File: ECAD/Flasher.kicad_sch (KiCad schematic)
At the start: 7 parts, among them Q1 BC817, Q2 BC817, U3 CH340C

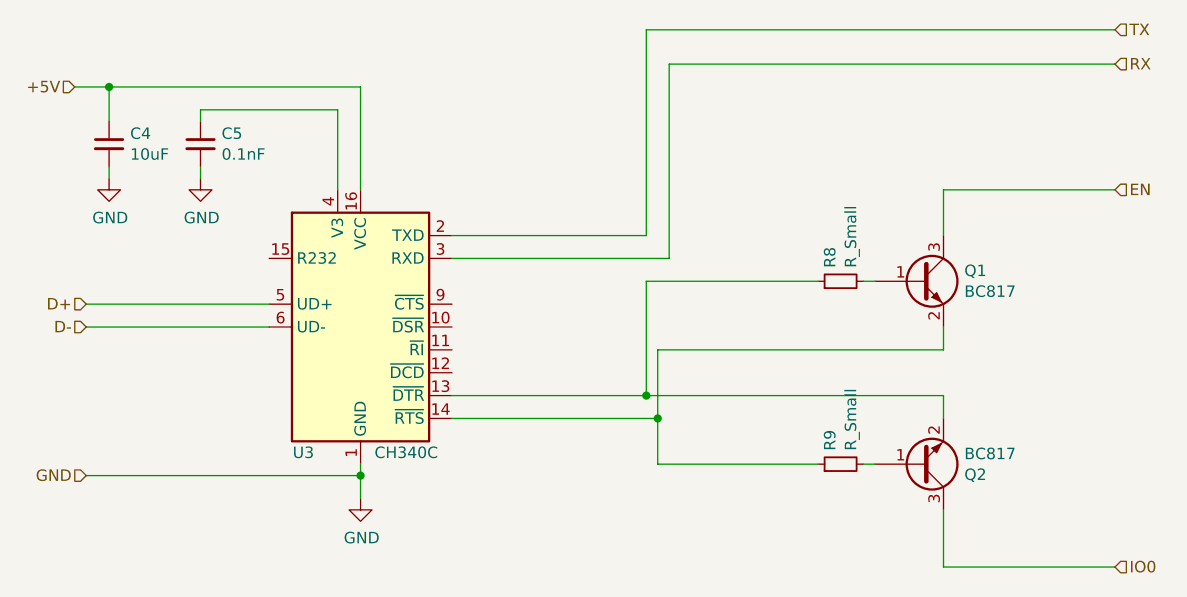
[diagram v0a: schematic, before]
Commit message: finishing up pcb, only billonly bill of materials need to be done to be compatible with lc from jlcpcb
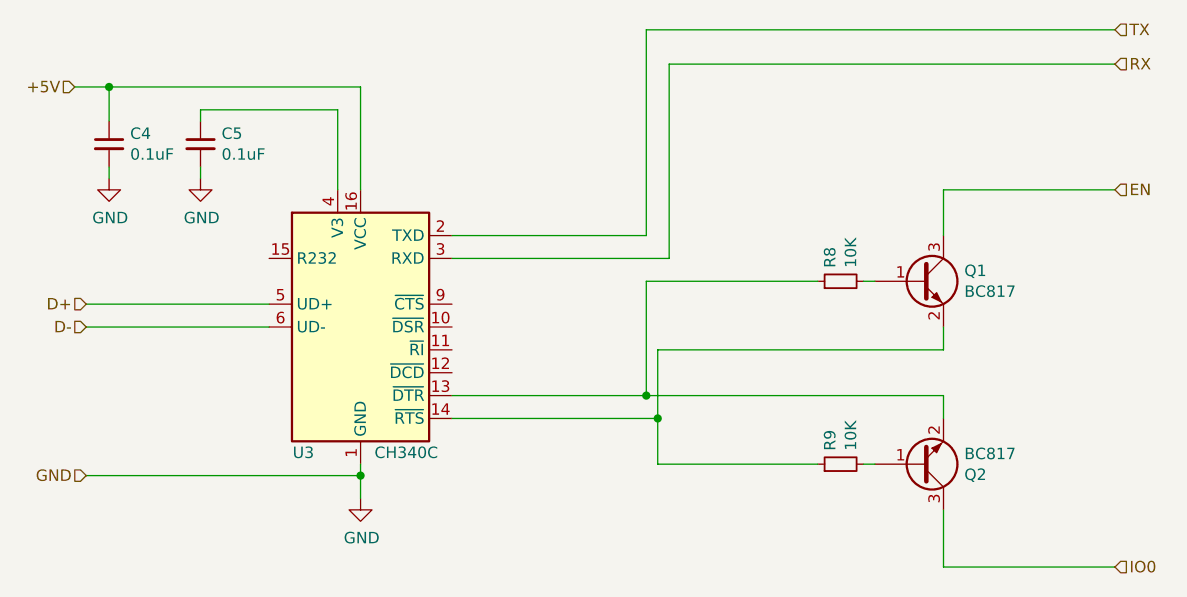
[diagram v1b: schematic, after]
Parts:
- C4: value 10uF -> 0.1uF
- C5: value 0.1nF -> 0.1uF
- R8, R9: value R_Small -> 10K
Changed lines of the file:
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@@
       (effects (font (size 1.27 1.27)) (justify left))
     )
-    (property "Value" "R_Small" (id 1) (at 129.413 79.7814 0)
+    (property "Value" "10K" (id 1) (at 129.413 79.781 0)
       (effects (font (size 1.27 1.27)) (justify left))
     )
@@
       (effects (font (size 1.27 1.27)) (justify left))
     )
-    (property "Value" "R_Small" (id 1) (at 129.413 100.1014 0)
+    (property "Value" "10K" (id 1) (at 129.413 100.1014 0)
       (effects (font (size 1.27 1.27)) (justify left))
     )
@@
       (effects (font (size 1.27 1.27)) (justify left))
     )
-    (property "Value" "10uF" (id 1) (at 49.3268 67.183 0)
+    (property "Value" "0.1uF" (id 1) (at 49.327 67.183 0)
       (effects (font (size 1.27 1.27)) (justify left))
     )
@@
       (effects (font (size 1.27 1.27)) (justify left))
     )
-    (property "Value" "0.1nF" (id 1) (at 59.4868 67.183 0)
+    (property "Value" "0.1uF" (id 1) (at 59.4868 67.183 0)
       (effects (font (size 1.27 1.27)) (justify left))
     )

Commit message: BOM fixed, ready to order
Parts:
- C4, C5: Manufacturer (none) -> CCTC; Manufacturer Number (none) -> TCC0603X7R104K500CT
- Q1, Q2: Manufacturer (none) -> ON Semiconductor; Manufacturer Number (none) -> BC818-40LT1G
- R8, R9: Manufacturer (none) -> UNI-ROYAL(Uniroyal Elec); Manufacturer Number (none) -> 0603WAF1002T5E
- U3: Manufacturer (none) -> WCH(Jiangsu Qin Heng); Manufacturer Number (none) -> CH340C
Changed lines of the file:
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@@
       (effects (font (size 1.27 1.27)) hide)
     )
-    (property "Datasheet" "~" (id 3) (at 128.27 81.28 0)
+    (property "Datasheet" "https://datasheet.lcsc.com/lcsc/1811062009_UNI-ROYAL-Uniroyal-Elec-0603WAF1002T5E_C25804.pdf" (id 3) (at 128.27 81.28 0)
+      (effects (font (size 1.27 1.27)) hide)
+    )
+    (property "Manufacturer" "UNI-ROYAL(Uniroyal Elec)" (id 4) (at 128.27 81.28 0)
+      (effects (font (size 1.27 1.27)) hide)
+    )
+    (property "Manufacturer Number" "0603WAF1002T5E" (id 5) (at 128.27 81.28 0)
       (effects (font (size 1.27 1.27)) hide)
     )
@@
       (effects (font (size 1.27 1.27)) hide)
     )
-    (property "Datasheet" "~" (id 3) (at 128.27 101.6 0)
+    (property "Datasheet" "https://datasheet.lcsc.com/lcsc/1811062009_UNI-ROYAL-Uniroyal-Elec-0603WAF1002T5E_C25804.pdf" (id 3) (at 128.27 101.6 0)
+      (effects (font (size 1.27 1.27)) hide)
+    )
+    (property "Manufacturer" "UNI-ROYAL(Uniroyal Elec)" (id 4) (at 128.27 101.6 0)
+      (effects (font (size 1.27 1.27)) hide)
+    )
+    (property "Manufacturer Number" "0603WAF1002T5E" (id 5) (at 128.27 101.6 0)
       (effects (font (size 1.27 1.27)) hide)
     )
@@
       (effects (font (size 1.27 1.27)) hide)
     )
-    (property "Datasheet" "~" (id 3) (at 46.99 66.04 0)
+    (property "Datasheet" "https://datasheet.lcsc.com/lcsc/1810181652_CCTC-TCC0603X7R104K500CT_C282519.pdf" (id 3) (at 46.99 66.04 0)
+      (effects (font (size 1.27 1.27)) hide)
+    )
+    (property "Manufacturer" "CCTC" (id 4) (at 46.99 66.04 0)
+      (effects (font (size 1.27 1.27)) hide)
+    )
+    (property "Manufacturer Number" "TCC0603X7R104K500CT" (id 5) (at 46.99 66.04 0)
       (effects (font (size 1.27 1.27)) hide)
     )
@@
       (effects (font (size 1.27 1.27)) hide)
     )
-    (property "Datasheet" "~" (id 3) (at 57.15 66.04 0)
+    (property "Datasheet" "https://datasheet.lcsc.com/lcsc/1810181652_CCTC-TCC0603X7R104K500CT_C282519.pdf" (id 3) (at 57.15 66.04 0)
+      (effects (font (size 1.27 1.27)) hide)
+    )
+    (property "Manufacturer" "CCTC" (id 4) (at 57.15 66.04 0)
+      (effects (font (size 1.27 1.27)) hide)
+    )
+    (property "Manufacturer Number" "TCC0603X7R104K500CT" (id 5) (at 57.15 66.04 0)
       (effects (font (size 1.27 1.27)) hide)
     )
@@
       (effects (font (size 1.27 1.27)) (justify left) hide)
     )
+    (property "Manufacturer" "	ON Semiconductor" (id 4) (at 137.16 81.28 0)
+      (effects (font (size 1.27 1.27)) hide)
+    )
+    (property "Manufacturer Number" "BC818-40LT1G" (id 5) (at 137.16 81.28 0)
+      (effects (font (size 1.27 1.27)) hide)
+    )
     (pin "1")
     (pin "2")
@@
       (effects (font (size 1.27 1.27)) (justify left) hide)
     )
+    (property "Manufacturer" "	ON Semiconductor" (id 4) (at 137.16 101.6 0)
+      (effects (font (size 1.27 1.27)) hide)
+    )
+    (property "Manufacturer Number" "BC818-40LT1G" (id 5) (at 137.16 101.6 0)
+      (effects (font (size 1.27 1.27)) hide)
+    )
     (pin "1")
     (pin "2")
@@
       (effects (font (size 1.27 1.27)) (justify left) hide)
     )
-    (property "Datasheet" "https://datasheet.lcsc.com/szlcsc/Jiangsu-Qin-Heng-CH340C_C84681.pdf" (id 3) (at 66.04 66.04 0)
+    (property "Datasheet" "https://datasheet.lcsc.com/lcsc/2008191806_WCH-Jiangsu-Qin-Heng-CH340C_C84681.pdf" (id 3) (at 66.04 66.04 0)
       (effects (font (size 1.27 1.27)) hide)
     )
+    (property "Manufacturer" "WCH(Jiangsu Qin Heng)" (id 4) (at 74.93 86.36 0)
+      (effects (font (size 1.27 1.27)) hide)
+    )
+    (property "Manufacturer Number" "CH340C" (id 5) (at 74.93 86.36 0)
+      (effects (font (size 1.27 1.27)) hide)
+    )

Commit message: adding production and step files
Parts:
- C4, C5, R8, R9: Package (none) -> 0603
- Q1, Q2: Package (none) -> SOT-23(SOT-23-3)
- U3: Package (none) -> SOP-16_150mil
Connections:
- no-connect marks 0 -> 5
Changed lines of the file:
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@@
   (junction (at 106.68 93.98) (diameter 0.9144) (color 0 0 0 0))
   (junction (at 107.95 96.52) (diameter 0.9144) (color 0 0 0 0))
+  (no_connect (at 64.77 78.74))
+  (no_connect (at 85.09 83.82))
+  (no_connect (at 85.09 86.36))
+  (no_connect (at 85.09 88.9))
+  (no_connect (at 85.09 91.44))
   (wire (pts (xy 44.45 102.87) (xy 74.93 102.87))
     (stroke (width 0) (type solid) (color 0 0 0 0))
@@
     (effects (font (size 1.27 1.27)) (justify right))
   )
-  (hierarchical_label "D+" (shape input) (at 44.45 83.82 180)
+  (hierarchical_label "D+" (shape bidirectional) (at 44.45 83.82 180)
     (effects (font (size 1.27 1.27)) (justify right))
   )
-  (hierarchical_label "D-" (shape input) (at 44.45 86.36 180)
+  (hierarchical_label "D-" (shape bidirectional) (at 44.45 86.36 180)
     (effects (font (size 1.27 1.27)) (justify right))
   )
@@
     (effects (font (size 1.27 1.27)) (justify right))
   )
-  (hierarchical_label "TX" (shape input) (at 158.75 53.34 0)
+  (hierarchical_label "TX" (shape output) (at 158.75 53.34 0)
     (effects (font (size 1.27 1.27)) (justify left))
   )
@@
     (effects (font (size 1.27 1.27)) (justify left))
   )
-  (hierarchical_label "EN" (shape input) (at 158.75 71.12 0)
+  (hierarchical_label "EN" (shape output) (at 158.75 71.12 0)
     (effects (font (size 1.27 1.27)) (justify left))
   )
-  (hierarchical_label "IO0" (shape input) (at 158.75 113.03 0)
+  (hierarchical_label "IO0" (shape output) (at 158.75 113.03 0)
     (effects (font (size 1.27 1.27)) (justify left))
   )
@@
       (effects (font (size 1.27 1.27)) hide)
     )
+    (property "Package" "0603" (id 4) (at 128.27 81.28 0)
+      (effects (font (size 1.27 1.27)) hide)
+    )
     (pin "1")
     (pin "2")
@@
       (effects (font (size 1.27 1.27)) hide)
     )
+    (property "Package" "0603" (id 4) (at 128.27 101.6 0)
+      (effects (font (size 1.27 1.27)) hide)
+    )
     (pin "1")
     (pin "2")
@@
       (effects (font (size 1.27 1.27)) hide)
     )
+    (property "Package" "0603" (id 4) (at 46.99 66.04 0)
+      (effects (font (size 1.27 1.27)) hide)
+    )
     (pin "1")
     (pin "2")
@@
     )
     (property "Manufacturer Number" "TCC0603X7R104K500CT" (id 5) (at 57.15 66.04 0)
+      (effects (font (size 1.27 1.27)) hide)
+    )
+    (property "Package" "0603" (id 4) (at 57.15 66.04 0)
       (effects (font (size 1.27 1.27)) hide)
     )
@@
       (effects (font (size 1.27 1.27)) hide)
     )
+    (property "Package" "SOT-23(SOT-23-3)" (id 4) (at 137.16 81.28 0)
+      (effects (font (size 1.27 1.27)) hide)
+    )
     (pin "1")
     (pin "2")
@@
     )
     (property "Manufacturer Number" "BC818-40LT1G" (id 5) (at 137.16 101.6 0)
+      (effects (font (size 1.27 1.27)) hide)
+    )
+    (property "Package" "SOT-23(SOT-23-3)" (id 4) (at 137.16 101.6 0)
       (effects (font (size 1.27 1.27)) hide)
     )
@@
       (effects (font (size 1.27 1.27)) hide)
     )
+    (property "Package" "SOP-16_150mil" (id 4) (at 74.93 86.36 0)
+      (effects (font (size 1.27 1.27)) hide)
+    )
